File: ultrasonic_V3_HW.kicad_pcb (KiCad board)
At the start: 2 copper layers, 206 parts, among them J1 Conn_02x20_Odd_Even, J2 Conn_Coaxial, J3 Conn_Coaxial, J4 Conn_01x07_Pin, J5 Screw_Terminal_01x02, J6 Conn_Coaxial, J7 Conn_Coaxial, Q10 NMOS, Q11 NMOS, Q12 NMOS, Q13 NMOS, Q14 NMOS, Q15 NMOS, Q16 NMOS, Q17 NMOS, Q18 NMOS, Q19 NMOS, Q2 NMOS, Q20 NMOS, Q21 NMOS, Q22 NMOS, Q3 NMOS, Q4 NMOS, Q5 NMOS, Q6 NMOS, Q7 NMOS, Q8 NMOS, Q9 NMOS, U1 MACHXO2-1200HC-4TG100C, U10 MIC4604YM, U11 MIC4604YM, U12 OKI-78SR-3.3_1.5-W36H-C, U13 OKI-78SR-12_1.0-W36H-C, U14 MCP1501-30xSN, U15 LM34966, U2 TDC_7200, U4 TLV3501AID, U5 DGS0010A, U6 OPA2392, U7 ADC10065, U8 MIC4604YM, U9 MIC4604YM, X1 16MHz

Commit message: schematic ready, basic layout done
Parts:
- removed NT1, NT2, NT3, NT4, NT5, NT6, NT7, NT8: NetTie_2, NetTie:NetTie-2_SMD_Pad0.5mm
- removed Q16, Q17, Q18, Q19, Q20, Q21: NMOS, Package_TO_SOT_SMD:SOT-23_Handsoldering
- added C14: 100n, Capacitor_SMD:C_0603_1608Metric_Pad1.08x0.95mm_HandSolder, B.Cu at (188.0, 92.4)
- added C15: 4u7, Capacitor_SMD:C_0805_2012Metric_Pad1.18x1.45mm_HandSolder, F.Cu at (149.4, 133.4)
- added C62: 4u7, Capacitor_SMD:C_0805_2012Metric_Pad1.18x1.45mm_HandSolder, F.Cu at (149.4, 130.3)
- added C63: 100n, Capacitor_SMD:C_0603_1608Metric_Pad1.08x0.95mm_HandSolder, F.Cu at (149.6, 128.4)
- added C64: 4u7, Capacitor_SMD:C_0805_2012Metric_Pad1.18x1.45mm_HandSolder, F.Cu at (208.5, 69.0)
- added C65: 4u7, Capacitor_SMD:C_0805_2012Metric_Pad1.18x1.45mm_HandSolder, F.Cu at (208.5, 72.0)
- added C66: 220n, Capacitor_SMD:C_0603_1608Metric_Pad1.08x0.95mm_HandSolder, F.Cu at (208.2, 65.8)
- added C67: 220n, Capacitor_SMD:C_0603_1608Metric_Pad1.08x0.95mm_HandSolder, F.Cu at (208.5, 115.0)
- added C68: 4u7, Capacitor_SMD:C_0805_2012Metric_Pad1.18x1.45mm_HandSolder, F.Cu at (208.5, 118.0)
- added C69: 4u7, Capacitor_SMD:C_0805_2012Metric_Pad1.18x1.45mm_HandSolder, F.Cu at (208.5, 121.0)
- added C70: 220n, Capacitor_SMD:C_0603_1608Metric_Pad1.08x0.95mm_HandSolder, F.Cu at (189.7, 125.2)
- added C71: 4u7, Capacitor_SMD:C_0805_2012Metric_Pad1.18x1.45mm_HandSolder, F.Cu at (189.5, 127.0)
- added C72: 220n, Capacitor_SMD:C_0603_1608Metric_Pad1.08x0.95mm_HandSolder, F.Cu at (173.9, 125.0)
- added C73: 4u7, Capacitor_SMD:C_0805_2012Metric_Pad1.18x1.45mm_HandSolder, F.Cu at (174.0, 127.0)
- added C74: 220n, Capacitor_SMD:C_0603_1608Metric_Pad1.08x0.95mm_HandSolder, F.Cu at (173.4, 52.9)
- added C75: 4u7, Capacitor_SMD:C_0805_2012Metric_Pad1.18x1.45mm_HandSolder, F.Cu at (173.5, 54.9)
- added C76: 220n, Capacitor_SMD:C_0603_1608Metric_Pad1.08x0.95mm_HandSolder, F.Cu at (189.5, 52.9)
- added C77: 4u7, Capacitor_SMD:C_0805_2012Metric_Pad1.18x1.45mm_HandSolder, F.Cu at (189.5, 54.9)
- added C78: 100n, Capacitor_SMD:C_0603_1608Metric_Pad1.08x0.95mm_HandSolder, B.Cu at (159.0, 101.5)
- added C79: 100n, Capacitor_SMD:C_0603_1608Metric_Pad1.08x0.95mm_HandSolder, B.Cu at (92.5, 82.0)
- added C80: 100n, Capacitor_SMD:C_0603_1608Metric_Pad1.08x0.95mm_HandSolder, B.Cu at (105.0, 82.5)
- added D24: LED_GREEN, LED_SMD:LED_0805_2012Metric_Pad1.15x1.40mm_HandSolder, F.Cu at (89.0, 67.5)
- added D26: LED_GREEN, LED_SMD:LED_0805_2012Metric_Pad1.15x1.40mm_HandSolder, F.Cu at (89.0, 64.6)
- added D27: LED_GREEN, LED_SMD:LED_0805_2012Metric_Pad1.15x1.40mm_HandSolder, F.Cu at (89.0, 61.6)
- added H1: MountingHole_Pad, MountingHole:MountingHole_3.2mm_M3_DIN965_Pad_TopBottom, F.Cu at (89.5, 49.5)
- added H2: MountingHole_Pad, MountingHole:MountingHole_3.2mm_M3_DIN965_Pad_TopBottom, F.Cu at (89.5, 139.5)
- added H3: MountingHole_Pad, MountingHole:MountingHole_3.2mm_M3_DIN965_Pad_TopBottom, F.Cu at (211.0, 139.5)
- added H4: MountingHole_Pad, MountingHole:MountingHole_3.2mm_M3_DIN965_Pad_TopBottom, F.Cu at (211.0, 49.5)
- added Q1: NMOS, Package_TO_SOT_SMD:SOT-23_Handsoldering, F.Cu at (193.0, 84.0)
- added R67: 10k, Resistor_SMD:R_0603_1608Metric_Pad0.98x0.95mm_HandSolder, F.Cu at (96.0, 61.6)
- added R68: 10k, Resistor_SMD:R_0603_1608Metric_Pad0.98x0.95mm_HandSolder, F.Cu at (89.5, 91.0)
- added R69: 10k, Resistor_SMD:R_0603_1608Metric_Pad0.98x0.95mm_HandSolder, F.Cu at (90.5, 88.5)
- added R70: 10k, Resistor_SMD:R_0603_1608Metric_Pad0.98x0.95mm_HandSolder, F.Cu at (91.5, 91.0)
- added U17: OPA388, Package_SO:VSSOP-8_3.0x3.0mm_P0.65mm, F.Cu at (167.1, 95.0)
- added U18: LM393, Package_SO:TSSOP-8_4.4x3mm_P0.65mm, F.Cu at (90.5, 83.0)
- added U3: MAX9939, SpecialStuff:uMAX 10 pin, F.Cu at (187.5, 92.5)
- C10: value 6u -> 100n; footprint Capacitor_SMD:C_0805_2012Metric_Pad1.18x1.45mm_HandSolder -> Capacitor_SMD:C_0603_1608Metric_Pad1.08x0.95mm_HandSolder
- C11, C8: value 15u -> 100n; footprint Capacitor_SMD:C_0805_2012Metric_Pad1.18x1.45mm_HandSolder -> Capacitor_SMD:C_0603_1608Metric_Pad1.08x0.95mm_HandSolder
- C12: value 100n -> 100p
- C13, C2, C26, C27, C28, C29, C30, C31, C32, C33, C53, C54, C55, C60, C7, R22, R60: moved to B.Cu
- C9: value 6u -> 100n; footprint Capacitor_SMD:C_0805_2012Metric_Pad1.18x1.45mm_HandSolder -> Capacitor_SMD:C_0603_1608Metric_Pad1.08x0.95mm_HandSolder; moved to B.Cu
- R10, R12: value 10k -> 1k
- R11, R9: value 10k -> 12
- R14: value 10k -> 100
- R15: value 10k -> 0; moved to B.Cu
- R16, R17, R18, R25: value 1k -> 0
- R19, R21, R24: value 1k -> 0; moved to B.Cu
- R23: value 1k -> 100
- R26: value 1k -> 10k
- R27, R44: value 3k3 -> 10k
- R28, R45: value 4k7 -> 10k
- R42, R46: value 6k8 -> 10k
- R43, R47: value 8k2 -> 10k
- U6: value OPA2392 -> LM339; footprint Package_SO:SOIC-8_3.9x4.9mm_P1.27mm -> Package_SO:TSSOP-14_4.4x5mm_P0.65mm
- moved F1 124.2 mm to (145.9, 138.5)
- moved U14 120.9 mm to (161.0, 110.5)
- moved C54 117.5 mm to (167.5, 109.6), turned to -90 degrees
- moved Q15 115.7 mm to (92.5, 74.0), turned to 90 degrees
- moved C55 114.9 mm to (165.5, 109.6), turned to -90 degrees
- moved C2 112.4 mm to (158.0, 109.1), turned to -90 degrees
- moved R58 111.2 mm to (101.5, 78.5), turned to 0 degrees
- moved R43 111.1 mm to (99.5, 88.1), turned to 0 degrees
- moved U6 109.9 mm to (102.5, 82.0)
- moved R42 109.4 mm to (98.5, 90.6)
- moved R44 109.2 mm to (100.5, 90.6)
- moved R45 108.9 mm to (97.0, 78.5), turned to 0 degrees
- moved C53 108.8 mm to (163.0, 109.6), turned to 90 degrees
- moved R47 108.3 mm to (92.5, 78.5), turned to 0 degrees
- moved Q6 107.7 mm to (97.0, 74.0), turned to 90 degrees
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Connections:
- net /H-bridges/A_signal renamed /H-bridges/BRIDGE_A_SIGNAL
- net /H-bridges/B_signal renamed /H-bridges/BRIDGE_B_SIGNAL
- net /PowerManagement/step-up/PHV renamed /PowerManagement/step-up/PHV_UNFUSED
- C10 pad 1: /AnalogFrontend/ProgrammableGain1/in -> Net-(U17A-+)
- C10 pad 2: Net-(U6B--) -> /AnalogFrontend/AMPLIFIED_SIGNAL_P
- C11 pad 2: Net-(U6B-+) -> GND
- C12 pad 1: /P3V3 -> /AnalogFrontend/SIGNAL_UNAMPLIFIED_P
- C12 pad 2: GND -> /AnalogFrontend/SIGNAL_UNAMPLIFIED_N
- C24 pad 2: /AnalogFrontend/AMPLIFIED_SIGNAL -> /AnalogFrontend/AMPLIFIED_SIGNAL_P
- C8 pad 1: /AnalogFrontend/SIGNAL_UNAMPLIFIED -> GND
- C8 pad 2: Net-(U6A-+) -> /AnalogFrontend/AMPLIFIED_SIGNAL_N
- C9 pad 1: /AnalogFrontend/ProgrammableGain0/in -> /P3V3
- C9 pad 2: Net-(U6A--) -> GND
- J3 pad 1: /H-bridges/C_signal -> /H-bridges/BRIDGE_C_SIGNAL
- J7 pad 1: /H-bridges/D_signal -> /H-bridges/BRIDGE_D_SIGNAL
- Q11 pad 3: /H-bridges/C_signal -> /H-bridges/BRIDGE_C_SIGNAL
- Q12 pad 1: /H-bridges/C_signal -> /H-bridges/BRIDGE_C_SIGNAL
- Q13 pad 3: /H-bridges/D_signal -> /H-bridges/BRIDGE_D_SIGNAL
- Q14 pad 1: /H-bridges/D_signal -> /H-bridges/BRIDGE_D_SIGNAL
- Q15 pad 1: Net-(Q15-D) -> Net-(D27-K)
- Q15 pad 2: /PGA_GATE2 -> Net-(Q15-G)
- Q2 pad 3: /AnalogFrontend/SIGNAL_UNAMPLIFIED -> /AnalogFrontend/SIGNAL_UNAMPLIFIED_N
- Q3 pad 1: /H-bridges/D_signal -> /H-bridges/BRIDGE_C_SIGNAL
- Q3 pad 3: /AnalogFrontend/SIGNAL_UNAMPLIFIED -> /AnalogFrontend/SIGNAL_UNAMPLIFIED_P
- Q4 pad 1: Net-(Q4-D) -> /H-bridges/BRIDGE_D_SIGNAL
- Q4 pad 2: /PGA_GATE20 -> Net-(Q4-G)
- Q4 pad 3: GND -> /AnalogFrontend/SIGNAL_UNAMPLIFIED_N
- Q5 pad 1: Net-(Q5-D) -> Net-(D24-K)
- Q5 pad 2: /PGA_GATE0 -> Net-(Q5-G)
- Q6 pad 1: Net-(Q6-D) -> Net-(D26-K)
- Q6 pad 2: /PGA_GATE1 -> Net-(Q6-G)
- R10 pad 1: /PGA_GATE21 -> Net-(Q1-G)
- R10 pad 2: GND -> /AnalogFrontend/SIGNAL_UNAMPLIFIED_P
- R11 pad 1: /PGA_GATE2 -> /fpga/EN_SIGNAL_D
- R11 pad 2: GND -> Net-(Q4-G)
- R12 pad 1: /PGA_GATE22 -> Net-(Q4-G)
- R12 pad 2: GND -> /AnalogFrontend/SIGNAL_UNAMPLIFIED_N
- R13 pad 2: /AnalogFrontend/SIGNAL_UNAMPLIFIED -> /AnalogFrontend/SIGNAL_UNAMPLIFIED_N
- R14 pad 1: /PGA_GATE3 -> /AnalogFrontend/AMPLIFIED_SIGNAL_N
- R14 pad 2: GND -> Net-(U7-VIN-)
- R15 pad 1: /PGA_GATE23 -> Net-(U7-IRS)
- R15 pad 2: GND -> /P3V3
- R16 pad 1: Net-(U6A-+) -> /AnalogFrontend/AMPLIFIED_SIGNAL
- R16 pad 2: /P3V_REF -> Net-(U17A--)
- R17 pad 1: GND -> Net-(C11-Pad1)
- R17 pad 2: Net-(U6A-+) -> Net-(U17A--)
- R18 pad 1: Net-(Q4-D) -> /AnalogFrontend/AMPLIFIED_SIGNAL
- R18 pad 2: /AnalogFrontend/ProgrammableGain1/in -> /AnalogFrontend/AMPLIFIED_SIGNAL_P
- R19 pad 1: Net-(U6B-+) -> /P3V_REF
- R19 pad 2: /P3V_REF -> Net-(U17A-+)
- R21 pad 1: /AnalogFrontend/AMPLIFIED_SIGNAL -> Net-(U17A-+)
- R21 pad 2: Net-(U6B--) -> GND
- R23 pad 1: /AnalogFrontend/AMPLIFIED_SIGNAL -> /AnalogFrontend/AMPLIFIED_SIGNAL_P
- R24 pad 1: Net-(C11-Pad1) -> Net-(U7-IRS)
- R24 pad 2: Net-(U6A--) -> GND
- R25 pad 1: GND -> Net-(U7-VCOM)
- R25 pad 2: Net-(U6B-+) -> Net-(U7-VIN-)
- R26 pad 1: Net-(Q5-D) -> Net-(U6B--)
- R26 pad 2: /AnalogFrontend/ProgrammableGain0/in -> GND
- R27 pad 1: Net-(Q6-D) -> Net-(U6A-+)
- R27 pad 2: /AnalogFrontend/ProgrammableGain0/in -> Net-(U6B--)
- R28 pad 1: Net-(Q15-D) -> /P3V3
- R28 pad 2: /AnalogFrontend/ProgrammableGain0/in -> Net-(U6A-+)
- R3 pad 2: /AnalogFrontend/SIGNAL_UNAMPLIFIED -> /AnalogFrontend/SIGNAL_UNAMPLIFIED_P
- R4 pad 1: /fpga/EN_SIGNAL_D -> /fpga/EN_SIGNAL_C
- R40 pad 2: /H-bridges/C_signal -> /H-bridges/BRIDGE_C_SIGNAL
- R41 pad 2: /H-bridges/D_signal -> /H-bridges/BRIDGE_D_SIGNAL
- R42 pad 1: Net-(Q16-D) -> /P12V
- R42 pad 2: /AnalogFrontend/ProgrammableGain0/in -> Net-(U6C-+)
- R43 pad 1: Net-(Q17-D) -> Net-(U6C-+)
- R43 pad 2: /AnalogFrontend/ProgrammableGain0/in -> Net-(U6D--)
- R44 pad 1: Net-(Q18-D) -> Net-(U6D--)
- R44 pad 2: /AnalogFrontend/ProgrammableGain1/in -> GND
- R45 pad 1: Net-(Q19-D) -> /P3V3
- R45 pad 2: /AnalogFrontend/ProgrammableGain1/in -> Net-(Q6-G)
- R46 pad 1: Net-(Q20-D) -> /P3V3
- R46 pad 2: /AnalogFrontend/ProgrammableGain1/in -> Net-(D26-A)
- R47 pad 1: Net-(Q21-D) -> /P3V3
- R47 pad 2: /AnalogFrontend/ProgrammableGain1/in -> Net-(Q15-G)
- R5 pad 1: /PGA_GATE0 -> /AnalogFrontend/AMPLIFIED_SIGNAL_P
- R5 pad 2: GND -> Net-(U3A-INB)
- R58 pad 1: /PGA_GATE4 -> /P3V3
- R58 pad 2: GND -> Net-(Q5-G)
- R59 pad 1: /PGA_GATE24 -> /P3V3
- R59 pad 2: GND -> Net-(D24-A)
- R8 pad 1: /PGA_GATE20 -> Net-(U3A-INB)
- R8 pad 2: GND -> /AnalogFrontend/AMPLIFIED_SIGNAL_N
- R9 pad 1: /PGA_GATE1 -> /fpga/EN_SIGNAL_A
- R9 pad 2: GND -> Net-(Q1-G)
- U1 pad 12: /fpga/SPI_LOCAL_SCK -> /SPI_LOCAL_SCK
- U1 pad 13: /fpga/TDC_CS -> unconnected-(U1D-PL5B/PCLKC3_1-Pad13)
- U1 pad 14: /DAC_CS -> unconnected-(U1D-PL5C-Pad14)
- U1 pad 15: /fpga/SRAM_CS -> unconnected-(U1D-PL5D-Pad15)
- U1 pad 16: /fpga/SPI_LOCAL_MOSI -> /SPI_LOCAL_MOSI
- U1 pad 17: /fpga/SPI_LOCAL_MISO -> /SPI_LOCAL_MISO
- U1 pad 35: /PGA_GATE0 -> unconnected-(U1C-PB9B/PCLKC2_0-Pad35)
- U1 pad 36: /PGA_GATE3 -> /fpga/SRAM_CS
- U1 pad 37: /PGA_GATE4 -> /AMP_CS
- U1 pad 38: /PGA_GATE1 -> /fpga/TDC_CS
- U1 pad 39: /PGA_GATE2 -> /DAC_CS
- U1 pad 41: /PGA_GATE20 -> unconnected-(U1C-PB15B-Pad41)
- U1 pad 42: /PGA_GATE21 -> /fpga/EN_SIGNAL_A
- U1 pad 43: /PGA_GATE22 -> /fpga/EN_SIGNAL_B
- U1 pad 45: /PGA_GATE23 -> /fpga/EN_SIGNAL_C
- U1 pad 47: /PGA_GATE24 -> /fpga/EN_SIGNAL_D
- U1 pad 91: /fpga/JTAG_TCK -> /JTAG_TCK
- U1 pad 94: /fpga/JTAG_TDI -> /JTAG_TDI
- U1 pad 95: /fpga/JTAG_TDO -> /JTAG_TDO
- U1 pad 98: /fpga/EN_SIGNAL_D -> unconnected-(U1A-PT9B-Pad98)
- U1 pad 99: /fpga/EN_SIGNAL_B -> unconnected-(U1A-PT9A-Pad99)
- U16 pad 2: /fpga/SRAM_MISO -> /SPI_LOCAL_MISO
- U16 pad 5: /fpga/SRAM_MOSI -> /SPI_LOCAL_MOSI
- U16 pad 6: /fpga/SRAM_SCLK -> /SPI_LOCAL_SCK
- U2 pad 10: /fpga/TDC_MOSI -> /SPI_LOCAL_MOSI
- U2 pad 12: /fpga/TDC_SCLK -> /SPI_LOCAL_SCK
- U2 pad 9: /fpga/TDC_MISO -> /SPI_LOCAL_MISO
- U5 pad 6: /DAC_SCLK -> /SPI_LOCAL_SCK
- U5 pad 8: /DAC_MOSI -> /SPI_LOCAL_MOSI
- U6 pad 1: Net-(C11-Pad1) -> Net-(Q5-G)
- U6 pad 2: Net-(U6A--) -> Net-(Q5-G)
- U6 pad 3: Net-(U6A-+) -> /P3V3
- U6 pad 4: GND -> /P3V_REF
- U6 pad 5: Net-(U6B-+) -> Net-(U6A-+)
- U6 pad 7: /AnalogFrontend/AMPLIFIED_SIGNAL -> /P3V_REF
- U6 pad 8: /P3V3 -> Net-(U6D--)
- U7 pad 12: Net-(U7-VCOM) -> Net-(U7-VIN-)
- U7 pad 5: /P3V3 -> Net-(U7-IRS)
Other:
- board outline added: 131.5 x 100 mm

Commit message: changed pins on fpga
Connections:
- U1 pad 13: unconnected-(U1D-PL5B/PCLKC3_1-Pad13) -> /fpga/TDC_STOP
- U1 pad 14: unconnected-(U1D-PL5C-Pad14) -> /fpga/TDC_START
- U1 pad 15: unconnected-(U1D-PL5D-Pad15) -> /fpga/TDC_TRIGG
- U1 pad 18: /fpga/PGOOD_HV_REGULATOR -> /fpga/TDC_EN
- U1 pad 19: /EN_HV_REGULATOR -> unconnected-(U1D-PL8D-Pad19)
- U1 pad 2: /fpga/SRAM_HOLD -> unconnected-(U1D-PL2D/L_GPLLC_IN-Pad2)
- U1 pad 20: /fpga/BRIDGE_A_HI -> unconnected-(U1D-PL9A/PCLKT3_0-Pad20)
- U1 pad 21: /fpga/BRIDGE_A_LO -> unconnected-(U1D-PL9B/PCLKC3_0-Pad21)
- U1 pad 24: /fpga/BRIDGE_B_HI -> /fpga/SRAM_CS
- U1 pad 25: /fpga/BRIDGE_B_LO -> /fpga/SRAM_HOLD
- U1 pad 27: /fpga/BRIDGE_C_HI -> unconnected-(U1C-PB4C/CSSPIN-Pad27)
- U1 pad 28: /fpga/BRIDGE_C_LO -> unconnected-(U1C-PB4D-Pad28)
- U1 pad 29: /fpga/BRIDGE_D_HI -> unconnected-(U1C-PB6A-Pad29)
- U1 pad 3: /COMP_SHT -> unconnected-(U1D-PL3A/PCLKT3_2-Pad3)
- U1 pad 30: /fpga/BRIDGE_D_HI -> unconnected-(U1C-PB6B-Pad30)
- U1 pad 34: unconnected-(U1C-PB9A/PCLKT2_0-Pad34) -> /fpga/PGOOD_HV_REGULATOR
- U1 pad 35: unconnected-(U1C-PB9B/PCLKC2_0-Pad35) -> /EN_HV_REGULATOR
- U1 pad 36: /fpga/SRAM_CS -> unconnected-(U1C-PB11C-Pad36)
- U1 pad 4: /fpga/TDC_STOP -> unconnected-(U1D-PL3B/PCLKC3_2-Pad4)
- U1 pad 40: unconnected-(U1C-PB15A-Pad40) -> /ADC_DF
- U1 pad 41: unconnected-(U1C-PB15B-Pad41) -> /ADC_STBY
- U1 pad 51: /LVDS_MOSI_N -> /fpga/BRIDGE_D_HI
- U1 pad 52: /LVDS_MOSI_P -> /fpga/BRIDGE_D_HI
- U1 pad 53: /LVDS_MISO_N -> /fpga/BRIDGE_C_LO
- U1 pad 54: /LVDS_MISO_P -> /fpga/BRIDGE_C_HI
- U1 pad 57: /LVDS_CS_N -> /COMP_SHT
- U1 pad 58: /LVDS_CS_P -> /STOP_SIGNAL
- U1 pad 59: /LVDS_SCLK_N -> /ADC_CLK
- U1 pad 60: /LVDS_SCLK_P -> /ADC_D0
- U1 pad 61: /ADC_STBY -> /ADC_D1
- U1 pad 62: /ADC_CLK -> /ADC_D2
- U1 pad 63: /ADC_DF -> /ADC_D3
- U1 pad 64: /ADC_D9 -> /ADC_D4
- U1 pad 65: /ADC_D8 -> /ADC_D5
- U1 pad 66: /ADC_D7 -> /ADC_D6
- U1 pad 67: /ADC_D6 -> /ADC_D7
- U1 pad 68: /ADC_D5 -> /ADC_D8
- U1 pad 69: /ADC_D4 -> /ADC_D9
- U1 pad 7: /fpga/TDC_START -> unconnected-(U1D-PL3C-Pad7)
- U1 pad 70: /ADC_D3 -> /fpga/BRIDGE_B_LO
- U1 pad 71: /ADC_D2 -> /fpga/BRIDGE_B_HI
- U1 pad 74: /ADC_D1 -> /fpga/BRIDGE_A_LO
- U1 pad 75: /ADC_D0 -> /fpga/BRIDGE_A_HI
- U1 pad 78: /fpga/STANBY_OSC -> unconnected-(U1A-PT16C-Pad78)
- U1 pad 8: /fpga/TDC_TRIGG -> unconnected-(U1D-PL3D-Pad8)
- U1 pad 83: unconnected-(U1A-PT15B-Pad83) -> /LVDS_MOSI_N
- U1 pad 84: unconnected-(U1A-PT15A-Pad84) -> /LVDS_MOSI_P
- U1 pad 87: unconnected-(U1A-PT12B/PCLKC0_1-Pad87) -> /LVDS_MISO_N
- U1 pad 88: unconnected-(U1A-PT12A/PCLKT0_1-Pad88) -> /LVDS_MISO_P
- U1 pad 9: /fpga/TDC_EN -> /fpga/STANBY_OSC
- U1 pad 96: unconnected-(U1A-PT10B-Pad96) -> /LVDS_CS_N
- U1 pad 97: /STOP_SIGNAL -> /LVDS_CS_P
- U1 pad 98: unconnected-(U1A-PT9B-Pad98) -> /LVDS_SCLK_N
- U1 pad 99: unconnected-(U1A-PT9A-Pad99) -> /LVDS_SCLK_P

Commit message: before changing MUX
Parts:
- added R71: 10k, Resistor_SMD:R_0603_1608Metric, F.Cu at (119.0, 93.2)
- added R72: 0, Resistor_SMD:R_0603_1608Metric_Pad0.98x0.95mm_HandSolder, F.Cu at (170.5, 97.7)
- C64, C65, C66, C67, C68, C69, R1, R2: moved to B.Cu
- moved Q14 28.5 mm to (172.0, 114.5)
- moved Q11 27.6 mm to (204.0, 114.5)
- moved C17 17.0 mm to (173.7, 132.3)
- moved C70 17.0 mm to (172.9, 127.9)
- moved D6 17.0 mm to (181.2, 125.2)
- moved R36 17.0 mm to (183.7, 125.2)
- moved R39 17.0 mm to (175.7, 125.1)
- moved R41 17.0 mm to (178.2, 125.2)
- moved C71 17.0 mm to (172.7, 129.7)
- moved U11 17.0 mm to (179.7, 131.2)
- moved C16 16.3 mm to (191.1, 132.2)
- moved C72 16.3 mm to (190.1, 127.5)
- moved C73 16.3 mm to (190.1, 129.6)
- moved D5 16.3 mm to (198.1, 125.0)
- moved R37 16.3 mm to (200.6, 125.0)
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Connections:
- R10 pad 2: /AnalogFrontend/SIGNAL_UNAMPLIFIED_P -> GND
- R12 pad 2: /AnalogFrontend/SIGNAL_UNAMPLIFIED_N -> GND
- R13 pad 2: /AnalogFrontend/SIGNAL_UNAMPLIFIED_N -> GND
- R16 pad 1: /AnalogFrontend/AMPLIFIED_SIGNAL -> Net-(R16-Pad1)
- R3 pad 2: /AnalogFrontend/SIGNAL_UNAMPLIFIED_P -> GND
- U1 pad 10: /fpga/TDC_INTB -> /SPI_LOCAL_MOSI
- U1 pad 13: /fpga/TDC_STOP -> /fpga/TDC_CS
- U1 pad 14: /fpga/TDC_START -> unconnected-(U1D-PL5C-Pad14)
- U1 pad 15: /fpga/TDC_TRIGG -> /fpga/TDC_STOP
- U1 pad 16: /SPI_LOCAL_MOSI -> /fpga/TDC_START
- U1 pad 17: /SPI_LOCAL_MISO -> /fpga/TDC_TRIGG
- U1 pad 20: unconnected-(U1D-PL9A/PCLKT3_0-Pad20) -> /fpga/SPI_FASTL_SCK
- U1 pad 21: unconnected-(U1D-PL9B/PCLKC3_0-Pad21) -> /fpga/SPI_FAST_MOSI
- U1 pad 25: /fpga/SRAM_HOLD -> /fpga/SPI_FAST_MISO
- U1 pad 27: unconnected-(U1C-PB4C/CSSPIN-Pad27) -> /fpga/SRAM_HOLD
- U1 pad 34: /fpga/PGOOD_HV_REGULATOR -> /EN_HV_REGULATOR
- U1 pad 35: /EN_HV_REGULATOR -> /fpga/PGOOD_HV_REGULATOR
- U1 pad 38: /fpga/TDC_CS -> unconnected-(U1C-PB11A/PCLKT2_1-Pad38)
- U1 pad 51: /fpga/BRIDGE_D_HI -> /fpga/BRIDGE_C_LO
- U1 pad 52: /fpga/BRIDGE_D_HI -> /fpga/BRIDGE_C_HI
- U1 pad 53: /fpga/BRIDGE_C_LO -> /fpga/BRIDGE_D_LO
- U1 pad 54: /fpga/BRIDGE_C_HI -> /fpga/BRIDGE_D_HI
- U1 pad 7: unconnected-(U1D-PL3C-Pad7) -> /fpga/STANBY_OSC
- U1 pad 8: unconnected-(U1D-PL3D-Pad8) -> /fpga/TDC_INTB
- U1 pad 9: /fpga/STANBY_OSC -> /SPI_LOCAL_MISO
- U11 pad 6: /fpga/BRIDGE_D_HI -> /fpga/BRIDGE_D_LO
- U16 pad 2: /SPI_LOCAL_MISO -> /fpga/SPI_FAST_MISO
- U16 pad 5: /SPI_LOCAL_MOSI -> /fpga/SPI_FAST_MOSI
- U16 pad 6: /SPI_LOCAL_SCK -> /fpga/SPI_FASTL_SCK
- U17 pad 6: /AnalogFrontend/AMPLIFIED_SIGNAL -> Net-(R16-Pad1)
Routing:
- net /SPI_LOCAL_MOSI: track 0.00 -> 117.1 mm, vias 0 -> 4
- net /SPI_LOCAL_SCK: track 0.00 -> 116.8 mm, vias 0 -> 5
- net /fpga/BRIDGE_A_HI: track 0.00 -> 89.4 mm
- net /fpga/BRIDGE_C_LO: track 0.00 -> 87.9 mm
- net /fpga/BRIDGE_A_LO: track 0.00 -> 87.0 mm
- net /fpga/BRIDGE_C_HI: track 0.00 -> 85.6 mm
- net /fpga/EN_SIGNAL_A: track 0.00 -> 82.6 mm, vias 0 -> 2
- net /fpga/EN_SIGNAL_B: track 0.00 -> 74.3 mm, vias 0 -> 2
- net /fpga/EN_SIGNAL_C: track 0.00 -> 73.0 mm, vias 0 -> 2
- net /fpga/BRIDGE_B_HI: track 0.00 -> 72.9 mm
- net /fpga/BRIDGE_B_LO: track 0.00 -> 70.4 mm
- net /fpga/BRIDGE_D_LO: track 0.00 -> 69.7 mm
- net /fpga/BRIDGE_D_HI: track 0.00 -> 67.6 mm
- net /fpga/EN_SIGNAL_D: track 0.00 -> 65.6 mm, vias 0 -> 2
- net /AMP_CS: track 0.00 -> 61.1 mm, vias 0 -> 2
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- added copper zone on In2.Cu, net GND
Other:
- board size 131.5 x 100 mm -> 130 x 100 mm
- copper layers 2 -> 4

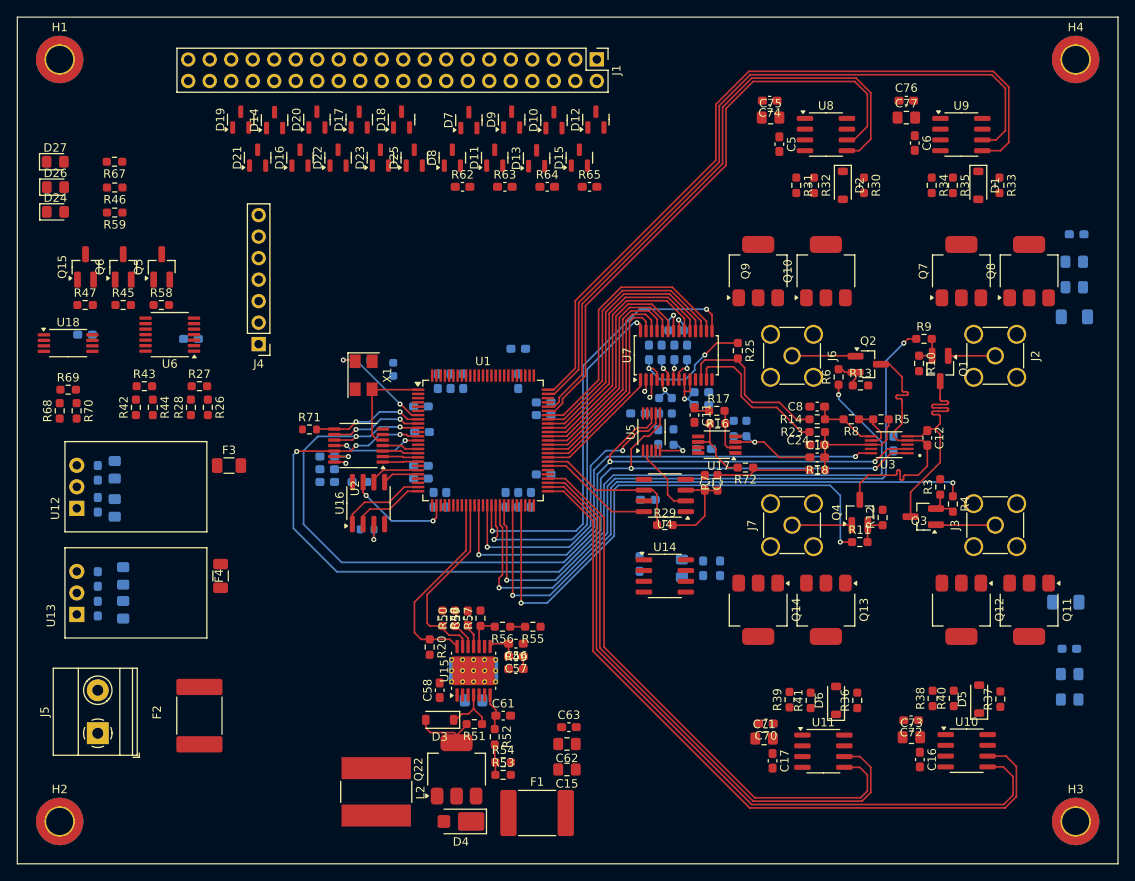
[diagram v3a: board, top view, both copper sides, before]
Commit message: no errors schematic, basic routing done
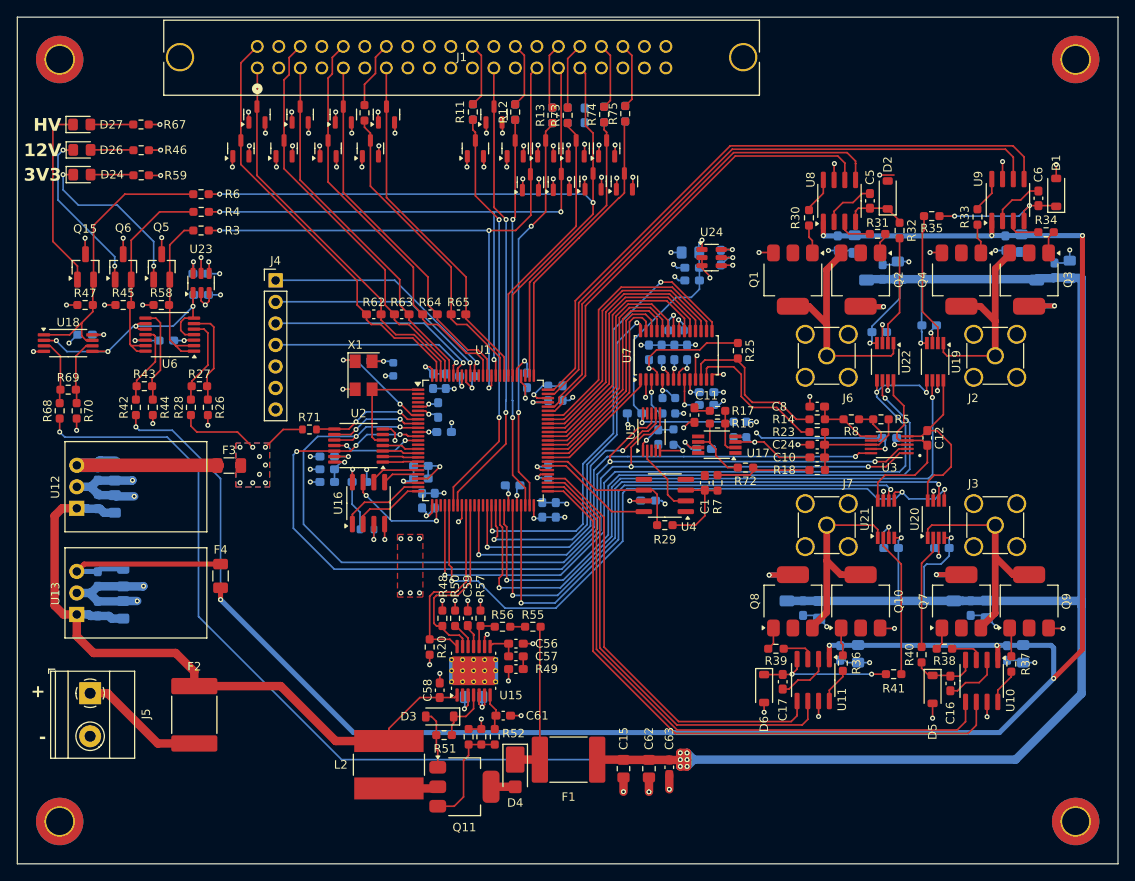
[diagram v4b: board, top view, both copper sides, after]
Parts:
- removed C2: 100n, Capacitor_SMD:C_0603_1608Metric_Pad1.08x0.95mm_HandSolder
- removed Q12, Q13, Q14, Q22: NMOS, Package_TO_SOT_SMD:SOT-223-3_TabPin2
- removed U14: MCP1501-30xSN, Package_SO:SOIC-8_3.9x4.9mm_P1.27mm
- added C81: 100n, Capacitor_SMD:C_0603_1608Metric_Pad1.08x0.95mm_HandSolder, B.Cu at (192.2, 80.9)
- added C82: 100n, Capacitor_SMD:C_0603_1608Metric_Pad1.08x0.95mm_HandSolder, B.Cu at (193.7, 107.2)
- added C83: 100n, Capacitor_SMD:C_0603_1608Metric_Pad1.08x0.95mm_HandSolder, B.Cu at (186.3, 81.7)
- added C84: 100n, Capacitor_SMD:C_0603_1608Metric_Pad1.08x0.95mm_HandSolder, B.Cu at (187.7, 107.2)
- added C85: 100n, Capacitor_SMD:C_0603_1608Metric_Pad1.08x0.95mm_HandSolder, B.Cu at (167.6, 72.9)
- added C86: 220n, Capacitor_SMD:C_0603_1608Metric_Pad1.08x0.95mm_HandSolder, B.Cu at (186.7, 74.6)
- added C87: 220n, Capacitor_SMD:C_0603_1608Metric_Pad1.08x0.95mm_HandSolder, B.Cu at (177.3, 114.3)
- added C88: 100n, Capacitor_SMD:C_0603_1608Metric_Pad1.08x0.95mm_HandSolder, B.Cu at (106.1, 74.8)
- added C89: 100n, Capacitor_SMD:C_0603_1608Metric_Pad1.08x0.95mm_HandSolder, B.Cu at (106.2, 77.3)
- added R73: 0, Resistor_SMD:R_0603_1608Metric_Pad0.98x0.95mm_HandSolder, F.Cu at (149.5, 56.1)
- added R74: 0, Resistor_SMD:R_0603_1608Metric_Pad0.98x0.95mm_HandSolder, F.Cu at (153.8, 56.0)
- added R75: 0, Resistor_SMD:R_0603_1608Metric_Pad0.98x0.95mm_HandSolder, F.Cu at (156.3, 55.9)
- added R76: 10k, Resistor_SMD:R_0603_1608Metric_Pad0.98x0.95mm_HandSolder, B.Cu at (147.7, 56.1)
- added R77: 10k, Resistor_SMD:R_0603_1608Metric_Pad0.98x0.95mm_HandSolder, B.Cu at (149.5, 56.1)
- added R78: 10k, Resistor_SMD:R_0603_1608Metric_Pad0.98x0.95mm_HandSolder, B.Cu at (153.8, 56.0)
- added R79: 10k, Resistor_SMD:R_0603_1608Metric_Pad0.98x0.95mm_HandSolder, B.Cu at (156.3, 55.9)
- added R80: 10k, Resistor_SMD:R_0603_1608Metric_Pad0.98x0.95mm_HandSolder, B.Cu at (138.3, 55.7)
- added R81: 10k, Resistor_SMD:R_0603_1608Metric_Pad0.98x0.95mm_HandSolder, B.Cu at (143.3, 55.7)
- added R82: 0, Resistor_SMD:R_0603_1608Metric_Pad0.98x0.95mm_HandSolder, F.Cu at (125.5, 55.8)
- added U19: ~, Package_SO:VSSOP-8_3.0x3.0mm_P0.65mm, F.Cu at (192.9, 85.2)
- added U20: ~, Package_SO:VSSOP-8_3.0x3.0mm_P0.65mm, F.Cu at (193.0, 103.8)
- added U21: ~, Package_SO:VSSOP-8_3.0x3.0mm_P0.65mm, F.Cu at (187.1, 103.8)
- added U22: ~, Package_SO:VSSOP-8_3.0x3.0mm_P0.65mm, F.Cu at (187.0, 85.2)
- added U23: MCP1501-25xCH, Package_TO_SOT_SMD:SOT-23-6, F.Cu at (106.2, 75.9)
- added U24: MCP1501-30xCH, Package_TO_SOT_SMD:SOT-23-6, F.Cu at (166.5, 72.9)
- C70, C71, C72, C73, C74, C75, C76, C77: moved to B.Cu
- J1: value Conn_02x20_Odd_Even -> 71918-140LF; footprint Connector_PinHeader_2.54mm:PinHeader_2x20_P2.54mm_Vertical -> SpecialStuff:CON40_2X20_USZ_FCI_GLE
- Q1, Q2, Q3, Q4: value NMOS -> DMN6069SE; footprint Package_TO_SOT_SMD:SOT-23_Handsoldering -> Package_TO_SOT_SMD:SOT-223-3_TabPin2
- Q10, Q11, Q7, Q8, Q9: value NMOS -> DMN6069SE
- R10: value 1k -> 0; footprint Resistor_SMD:R_0603_1608Metric_Pad0.98x0.95mm_HandSolder -> Resistor_SMD:R_1206_3216Metric_Pad1.30x1.75mm_HandSolder; moved to B.Cu
- R11, R4, R6: value 12 -> 0
- R12, R13, R3: value 1k -> 0
- R9: value 12 -> 0; footprint Resistor_SMD:R_0603_1608Metric_Pad0.98x0.95mm_HandSolder -> Resistor_SMD:R_1206_3216Metric_Pad1.30x1.75mm_HandSolder; moved to B.Cu
- moved R4 95.3 mm to (106.2, 67.5), turned to 0 degrees
- moved R3 92.4 mm to (106.2, 69.7), turned to 0 degrees
- moved R6 78.3 mm to (106.2, 65.4), turned to 0 degrees
- moved Q11 69.9 mm to (137.3, 135.4), turned to 0 degrees
- moved R11 68.3 mm to (138.3, 55.7), turned to 90 degrees
- moved R12 64.6 mm to (143.3, 55.7)
- moved Q9 50.4 mm to (204.0, 113.5)
- moved R13 48.4 mm to (147.7, 56.1), turned to 90 degrees
- moved Q8 48.0 mm to (176.1, 113.5)
- moved J1 40.1 mm to (112.8, 48.0), turned to 0 degrees
- moved Q10 39.2 mm to (184.1, 113.5)
- moved Q7 39.0 mm to (196.0, 113.5)
- moved C53 37.3 mm to (164.0, 72.3), turned to 0 degrees
- moved D21 36.0 mm to (148.8, 64.0)
- moved C55 35.5 mm to (164.2, 74.1), turned to 180 degrees
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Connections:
- J1 pad 1: /LVDS_MOSI_P -> /LVDS_SCLK_N
- J1 pad 10: /LVDS_CS_N -> unconnected-(J1A-Pin_10-Pad10)
- J1 pad 11: unconnected-(J1-Pin_11-Pad11) -> GND
- J1 pad 12: unconnected-(J1-Pin_12-Pad12) -> /CNTRL_MISO
- J1 pad 13: /LVDS_SCLK_P -> unconnected-(J1A-Pin_13-Pad13)
- J1 pad 14: /LVDS_SCLK_N -> /CNTRL_GPIO5
- J1 pad 15: unconnected-(J1-Pin_15-Pad15) -> /CNTRL_GPIO4
- J1 pad 16: unconnected-(J1-Pin_16-Pad16) -> /CNTRL_GPIO2
- J1 pad 18: GND -> /P3V3
- J1 pad 19: /CNTRL_GPIO0 -> GND
- J1 pad 2: /LVDS_MOSI_N -> unconnected-(J1A-Pin_2-Pad2)
- J1 pad 20: /CNTRL_MOSI -> GND
- J1 pad 21: /CNTRL_GPIO1 -> GND
- J1 pad 23: GND -> Net-(J1A-Pin_23)
- J1 pad 24: /CNTRL_MISO -> Net-(J1A-Pin_24)
- J1 pad 25: /CNTRL_GPIO2 -> Net-(J1A-Pin_25)
- J1 pad 26: GND -> Net-(J1A-Pin_26)
- J1 pad 27: /CNTRL_GPIO3 -> GND
- J1 pad 28: /CNTRL_CS -> Net-(J1A-Pin_28)
- J1 pad 3: unconnected-(J1-Pin_3-Pad3) -> /LVDS_CS_N
- J1 pad 30: GND -> Net-(J1A-Pin_30)
- J1 pad 31: /CNTRL_GPIO4 -> GND
- J1 pad 32: /CNTRL_SCLK -> unconnected-(J1A-Pin_32-Pad32)
- J1 pad 33: /CNTRL_GPIO5 -> unconnected-(J1A-Pin_33-Pad33)
- J1 pad 34: GND -> Net-(J1A-Pin_34)
- J1 pad 35: GND -> unconnected-(J1A-Pin_35-Pad35)
- J1 pad 36: /P3V3 -> /LVDS_MISO_P
- J1 pad 37: /P12V -> unconnected-(J1A-Pin_37-Pad37)
- J1 pad 38: GND -> /LVDS_CS_P
- J1 pad 39: GND -> unconnected-(J1A-Pin_39-Pad39)
- J1 pad 40: /PHV -> /LVDS_SCLK_P
- J1 pad 5: /LVDS_MISO_P -> /LVDS_MISO_N
- J1 pad 6: /LVDS_MISO_N -> unconnected-(J1A-Pin_6-Pad6)
- J1 pad 7: unconnected-(J1-Pin_7-Pad7) -> /LVDS_MOSI_N
- J1 pad 9: /LVDS_CS_P -> GND
- J2 pad 1: /H-bridges/BRIDGE_A_SIGNAL -> Net-(J2-In)
- J3 pad 1: /H-bridges/BRIDGE_C_SIGNAL -> Net-(J3-In)
- J4 pad 3: /JTAG_TDO -> /JTAG_TDI
- J4 pad 4: /JTAG_TDI -> /JTAG_TDO
- J6 pad 1: /H-bridges/BRIDGE_B_SIGNAL -> Net-(J6-In)
- J7 pad 1: /H-bridges/BRIDGE_D_SIGNAL -> Net-(J7-In)
- Q1 pad 1: /H-bridges/BRIDGE_A_SIGNAL -> /H-bridges/LB_GATE
- Q1 pad 2: Net-(Q1-G) -> Net-(J6-In)
- Q1 pad 3: /AnalogFrontend/SIGNAL_UNAMPLIFIED_P -> GND
- Q10 pad 1: /H-bridges/BRIDGE_B_SIGNAL -> /H-bridges/LD_GATE
- Q10 pad 2: /H-bridges/LB_GATE -> Net-(J7-In)
- Q11 pad 1: Net-(Q11-D) -> Net-(D3-A)
- Q11 pad 2: /H-bridges/HC_GATE -> Net-(D4-A)
- Q11 pad 3: /H-bridges/BRIDGE_C_SIGNAL -> Net-(Q11-S)
- Q15 pad 2: Net-(Q15-G) -> /P_GOOD_PHV
- Q2 pad 1: /H-bridges/BRIDGE_B_SIGNAL -> /H-bridges/HB_GATE
- Q2 pad 2: Net-(Q2-G) -> Net-(Q2-D)
- Q2 pad 3: /AnalogFrontend/SIGNAL_UNAMPLIFIED_N -> Net-(J6-In)
- Q3 pad 1: /H-bridges/BRIDGE_C_SIGNAL -> /H-bridges/HA_GATE
- Q3 pad 2: Net-(Q3-G) -> Net-(Q3-D)
- Q3 pad 3: /AnalogFrontend/SIGNAL_UNAMPLIFIED_P -> Net-(J2-In)
- Q4 pad 1: /H-bridges/BRIDGE_D_SIGNAL -> /H-bridges/LA_GATE
- Q4 pad 2: Net-(Q4-G) -> Net-(J2-In)
- Q4 pad 3: /AnalogFrontend/SIGNAL_UNAMPLIFIED_N -> GND
- Q5 pad 2: Net-(Q5-G) -> /P_GOOD_P3V3
- Q6 pad 2: Net-(Q6-G) -> /P_GOOD_P12V
- Q7 pad 1: Net-(Q7-D) -> /H-bridges/HC_GATE
- Q7 pad 2: /H-bridges/HA_GATE -> Net-(Q7-D)
- Q7 pad 3: /H-bridges/BRIDGE_A_SIGNAL -> Net-(J3-In)
- Q8 pad 1: /H-bridges/BRIDGE_A_SIGNAL -> /H-bridges/HD_GATE
- Q8 pad 2: /H-bridges/LA_GATE -> Net-(Q8-D)
- Q8 pad 3: GND -> Net-(J7-In)
- Q9 pad 1: Net-(Q7-D) -> /H-bridges/LC_GATE
- Q9 pad 2: /H-bridges/HB_GATE -> Net-(J3-In)
- Q9 pad 3: /H-bridges/BRIDGE_B_SIGNAL -> GND
- R1 pad 1: /PHV -> Net-(Q7-D)
- R1 pad 2: Net-(Q11-D) -> /PHV
- R10 pad 1: Net-(Q1-G) -> Net-(Q8-D)
- R10 pad 2: GND -> /PHV
- R11 pad 1: /fpga/EN_SIGNAL_D -> /CNTRL_SCLK
- R11 pad 2: Net-(Q4-G) -> Net-(J1A-Pin_30)
- R12 pad 1: Net-(Q4-G) -> /CNTRL_CS
- R12 pad 2: GND -> Net-(J1A-Pin_28)
- R13 pad 1: Net-(Q2-G) -> /CNTRL_MOSI
- R13 pad 2: GND -> Net-(J1A-Pin_26)
- R2 pad 1: /PHV -> Net-(Q3-D)
- R2 pad 2: Net-(Q7-D) -> /PHV
- R3 pad 1: Net-(Q3-G) -> /P_GOOD_P3V3
- R3 pad 2: GND -> /CNTRL_GPIO5
- R32 pad 2: /H-bridges/BRIDGE_B_SIGNAL -> /H-bridges/BRIDGE_B_MIDDLE
- R35 pad 2: /H-bridges/BRIDGE_A_SIGNAL -> /H-bridges/BRIDGE_A_MIDDLE
- R4 pad 1: /fpga/EN_SIGNAL_C -> /P_GOOD_P12V
- R4 pad 2: Net-(Q3-G) -> /CNTRL_GPIO4
- R40 pad 2: /H-bridges/BRIDGE_C_SIGNAL -> /H-bridges/BRIDGE_C_MIDDLE
- R41 pad 2: /H-bridges/BRIDGE_D_SIGNAL -> /H-bridges/BRIDGE_D_MIDDLE
- R45 pad 2: Net-(Q6-G) -> /P_GOOD_P12V
- R47 pad 2: Net-(Q15-G) -> /P_GOOD_PHV
- R52 pad 2: Net-(Q22-S) -> Net-(Q11-S)
- R53 pad 1: Net-(Q22-S) -> Net-(Q11-S)
- R54 pad 1: Net-(Q22-S) -> Net-(Q11-S)
- R58 pad 2: Net-(Q5-G) -> /P_GOOD_P3V3
- R6 pad 1: /fpga/EN_SIGNAL_B -> /P_GOOD_PHV
- R6 pad 2: Net-(Q2-G) -> /CNTRL_GPIO2
- R9 pad 1: /fpga/EN_SIGNAL_A -> Net-(Q2-D)
- R9 pad 2: Net-(Q1-G) -> /PHV
- U1 pad 29: unconnected-(U1C-PB6A-Pad29) -> /H-bridges/BRIDGE_AB_MUX_EN
- U1 pad 30: unconnected-(U1C-PB6B-Pad30) -> /H-bridges/BRIDGE_CD_MUX_EN
- U1 pad 42: /fpga/EN_SIGNAL_A -> /fpga/BRIDGE_A_SEL
- U1 pad 43: /fpga/EN_SIGNAL_B -> /fpga/BRIDGE_B_SEL
- U1 pad 45: /fpga/EN_SIGNAL_C -> /fpga/BRIDGE_C_SEL
- U1 pad 47: /fpga/EN_SIGNAL_D -> /fpga/BRIDGE_D_SEL
- U18 pad 1: Net-(Q15-G) -> /P_GOOD_PHV
- U18 pad 2: /P3V_REF -> /PowerManagement/P2V5_REF
- U18 pad 5: /P3V_REF -> /PowerManagement/P2V5_REF
- U18 pad 7: Net-(Q15-G) -> /P_GOOD_PHV
- U6 pad 1: Net-(Q5-G) -> /P_GOOD_P3V3
- U6 pad 10: /P3V_REF -> /PowerManagement/P2V5_REF
- U6 pad 13: Net-(Q6-G) -> /P_GOOD_P12V
- U6 pad 14: Net-(Q6-G) -> /P_GOOD_P12V
- U6 pad 2: Net-(Q5-G) -> /P_GOOD_P3V3
- U6 pad 4: /P3V_REF -> /PowerManagement/P2V5_REF
- U6 pad 7: /P3V_REF -> /PowerManagement/P2V5_REF
- U6 pad 9: /P3V_REF -> /PowerManagement/P2V5_REF
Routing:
- net /PHV: track 0.00 -> 322.3 mm, vias 0 -> 11
- net /P12V: track 0.00 -> 259.1 mm, vias 0 -> 8
- net GND: track 5.04 -> 253.4 mm, vias 2 -> 117
- net /P3V3: track 14.0 -> 169.0 mm, vias 4 -> 73
- net /H-bridges/BRIDGE_AB_MUX_EN: track 0.00 -> 90.8 mm, vias 0 -> 3
- net /CNTRL_GPIO2: track 0.00 -> 86.8 mm, vias 0 -> 2
- net /PowerManagement/P15V-20V_5S_FUSED: track 0.00 -> 83.8 mm
- net /H-bridges/BRIDGE_CD_MUX_EN: track 0.00 -> 82.6 mm, vias 0 -> 3
- net /fpga/EN_SIGNAL_A: track 82.6 -> 0.00 mm, vias 2 -> 0
- net /fpga/BRIDGE_A_SEL: track 0.00 -> 81.2 mm, vias 0 -> 2
- net /CNTRL_GPIO4: track 0.00 -> 78.3 mm, vias 0 -> 3
- net /fpga/BRIDGE_B_SEL: track 0.00 -> 77.2 mm, vias 0 -> 2
- net /CNTRL_GPIO5: track 0.00 -> 76.7 mm, vias 0 -> 3
- net /fpga/EN_SIGNAL_B: track 74.3 -> 0.00 mm, vias 2 -> 0
- net /fpga/EN_SIGNAL_C: track 73.0 -> 0.00 mm, vias 2 -> 0
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- added copper zone on B.Cu, net /P3V3
- added copper zone on F.Cu, net /P3V3
- added copper zone on In2.Cu, net /P3V3
- added copper zone on In1.Cu, net GND
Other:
- board text added: "+"
- board text added: "-"
- board text added: "12V"
- board text added: "3V3"
- board text added: "HV"
